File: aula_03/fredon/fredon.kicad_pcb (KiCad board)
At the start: 2 copper layers, 11 parts, among them J1 FRDM-KL25Z, J3 encoder1, J4 encoder2, J5 Conn_01x02_Socket, J6 Conn_01x06_Socket, U1 HC-SR04, U2 NRF24L01_10PIN

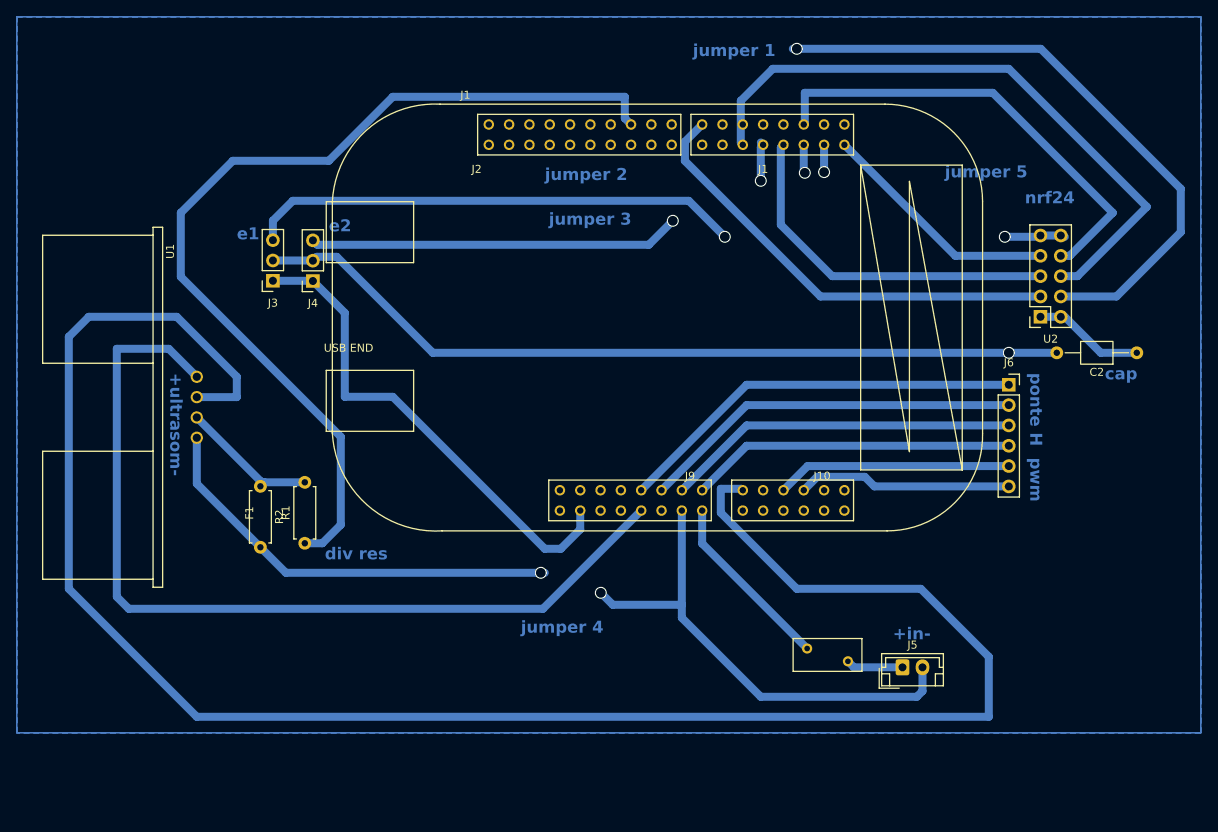
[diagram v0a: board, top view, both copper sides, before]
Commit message: feat(pcb): atualização da pcb para o tamanho de 10x10
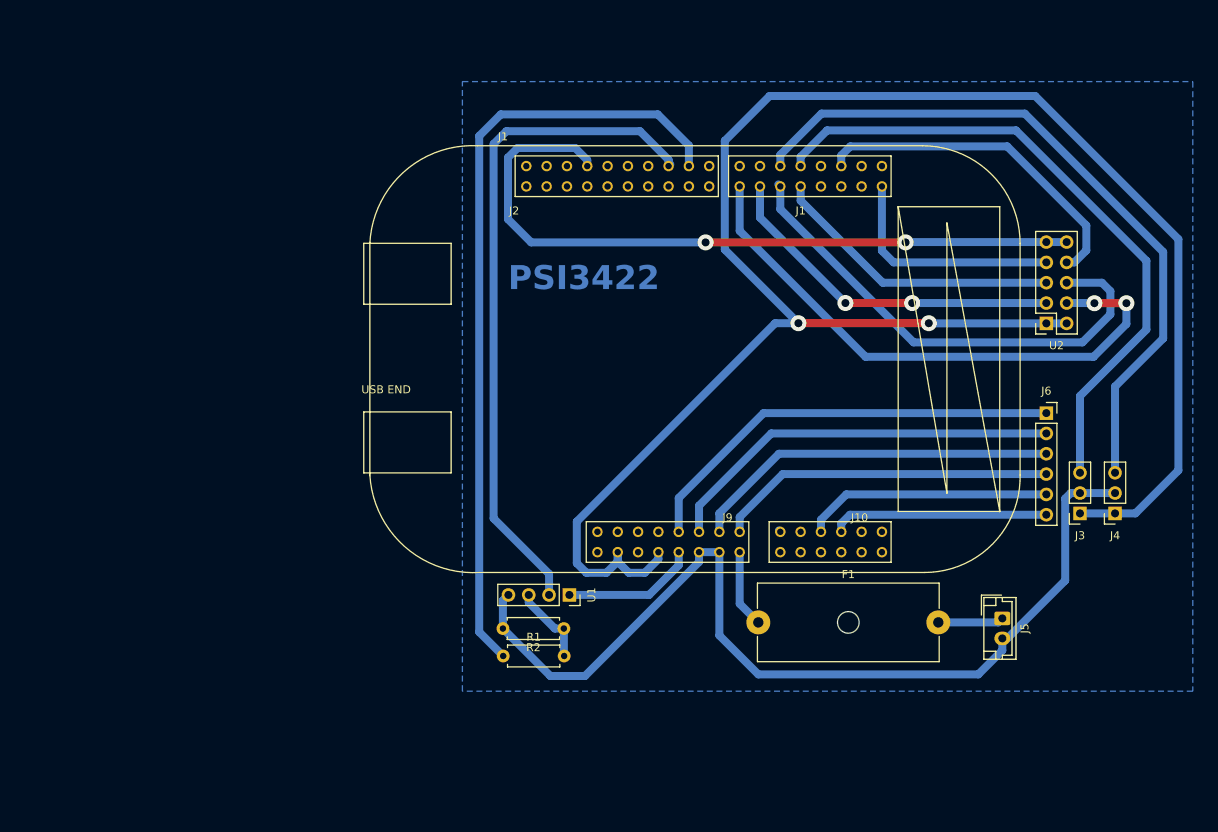
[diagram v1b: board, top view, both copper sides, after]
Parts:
- removed C2: C_Small, Capacitor_THT:C_Axial_L3.8mm_D2.6mm_P10.00mm_Horizontal
- F1: footprint Fuse:Fuse_BelFuse_0ZRE0005FF_L8.3mm_W3.8mm -> Fuse:Fuseholder_Cylinder-5x20mm_Schurter_0031_8201_Horizontal_Open
- U1: footprint HC-SR04:XCVR_HC-SR04 -> Connector_PinSocket_2.54mm:PinSocket_1x04_P2.54mm_Vertical
- moved J3 105.0 mm to (172.9, 102.6)
- moved J4 104.4 mm to (177.3, 102.6)
- moved U1 52.1 mm to (109.1, 112.8)
- moved R2 41.9 mm to (108.4, 117.0), turned to 180 degrees
- moved R1 28.5 mm to (100.8, 120.4), turned to 0 degrees
- moved J5 13.9 mm to (163.2, 115.7), turned to -90 degrees
- moved J1 7.00 mm to (124.5, 83.3)
- moved F1 6.92 mm to (132.7, 116.2)
- moved J6 5.88 mm to (168.7, 90.0)
- moved U2 1.10 mm to (168.7, 78.8)
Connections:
- net Net-(J1-P5V_USB) renamed +5V
- net Net-(J1-PTC6) renamed /PTC6
- net Net-(J1-PTC7) renamed /PTC7
- net Net-(J1-PTD4) renamed /PTD4
- net Net-(J1-PTE2) renamed /PTE2
- net Net-(J1-PTE22) renamed /PTE22
- net Net-(J1-PTE23) renamed /PTE23
- net Net-(J1-PTE3) renamed /PTE3
- net Net-(J1-PTE4) renamed /PTE4
- net Net-(J1-PTE5) renamed /PTE5
- J1 pad J1-10: unconnected-(J1-PTA4-PadJ1-10) -> /PTA4
- J1 pad J1-12: unconnected-(J1-PTA5-PadJ1-12) -> /PTA5
- J1 pad J1-13: unconnected-(J1-PTC10-PadJ1-13) -> /PTC10
- J1 pad J1-15: unconnected-(J1-PTC11-PadJ1-15) -> /PTC11
- J1 pad J1-16: Net-(J1-PTC9) -> unconnected-(J1-PTC9-PadJ1-16)
- J1 pad J1-3: Net-(J1-PTC0) -> unconnected-(J1-PTC0-PadJ1-3)
- J1 pad J1-5: Net-(J1-PTC3) -> unconnected-(J1-PTC3-PadJ1-5)
- J1 pad J1-7: Net-(J1-PTC4) -> unconnected-(J1-PTC4-PadJ1-7)
- J1 pad J1-9: Net-(J1-PTC5) -> /PTC5
- J1 pad J10-1: Net-(J1-PTE20) -> unconnected-(J1-PTE20-PadJ10-1)
- J1 pad J2-4: unconnected-(J1-PTD5-PadJ2-4) -> /PTD5
- J1 pad J2-6: Net-(J1-PTD0) -> /PTD0
- J1 pad J9-4: Net-(J3-Pin_1) -> +3.3V
- J1 pad J9-8: Net-(J3-Pin_1) -> +3.3V
- J3 pad 1: Net-(J3-Pin_1) -> +3.3V
- J3 pad 3: Net-(J1-PTC0) -> /PTA4
- J4 pad 1: Net-(J3-Pin_1) -> +3.3V
- J4 pad 3: Net-(J1-PTC3) -> /PTA5
- R1 pad 1: Net-(J1-PTD0) -> /PTD5
- U1 pad 2: Net-(J1-PTE20) -> /PTD0
- U2 pad 1: Net-(C2-Pad1) -> +3.3V
- U2 pad 2: Net-(C2-Pad1) -> +3.3V
- U2 pad 3: Net-(J1-PTC9) -> /PTC10
- U2 pad 4: Net-(J1-PTC5) -> /PTC11
- U2 pad 5: Net-(J1-PTC4) -> /PTC5
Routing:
- net Net-(J1-PTE20): track 240.1 -> 0.00 mm
- net +3.3V: track 0.00 -> 229.3 mm, vias 0 -> 2
- net Net-(J1-PTD0): track 118.0 -> 0.00 mm
- net /PTD5: track 0.00 -> 97.8 mm
- net +5V: track 113.7 -> 16.8 mm
- net /PTA5: track 0.00 -> 88.7 mm
- net Net-(J1-PTC5): track 84.5 -> 0.00 mm, vias 2 -> 0
- net /PTD0: track 0.00 -> 84.4 mm
- net /PTA4: track 0.00 -> 82.5 mm
- net /PTC11: track 0.00 -> 71.5 mm, vias 0 -> 2
- net Net-(J1-PTC0): track 65.2 -> 0.00 mm, vias 2 -> 0
- net Net-(J3-Pin_1): track 61.8 -> 0.00 mm
- net Net-(J1-PTC9): track 56.9 -> 0.00 mm
- net Net-(J1-PTC3): track 50.0 -> 0.00 mm, vias 2 -> 0
- net Net-(J1-PTC4): track 45.3 -> 0.00 mm
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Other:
- board text added: "PSI3422"
- board text removed: "+in-"
- board text removed: "+ultrasom-"
- board text removed: "cap"
- board text removed: "div res"
- board text removed: "e1"
- board text removed: "e2"
- board text removed: "jumper 1"
- board text removed: "jumper 2"
- board text removed: "jumper 3"
- board text removed: "jumper 4"
- board text removed: "jumper 5"
- board text removed: "nrf24"
- board text removed: "ponte H pwm"

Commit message: revisao da PCB
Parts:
- removed F1: Fuse, Fuse:Fuseholder_Cylinder-5x20mm_Schurter_0031_8201_Horizontal_Open
- U1: footprint Connector_PinSocket_2.54mm:PinSocket_1x04_P2.54mm_Vertical -> HC-SR04:XCVR_HC-SR04
- moved R1 15.8 mm to (116.5, 122.5)
- moved R2 15.8 mm to (124.1, 118.5)
- moved U1 5.60 mm to (111.5, 117.8)
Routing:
- net GND: track 209.8 -> 178.8 mm
- net /PTD5: track 97.8 -> 115.2 mm
- net Net-(U1-ECHO): track 10.1 -> 24.2 mm
- net /PTD0: track 84.4 -> 90.2 mm
- net +5V: track 16.8 -> 14.9 mm
- net +3.3V: track 229.3 -> 228.5 mm
- net Net-(J5-Pin_1): vias 0 -> 1
- net Net-(J1-P5-9V_VIN): vias 0 -> 1
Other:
- board text added: "e1"
- board text added: "e2"
- board text added: "nrf"
- board text added: "ponte H"

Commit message: relatorio
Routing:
- net GND: track 178.8 -> 201.3 mm, vias 2 -> 4
- net Net-(U1-ECHO): track 24.2 -> 18.5 mm
- net /PTD0: track 90.2 -> 91.6 mm
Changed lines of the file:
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@@
 			(at -3.81 0 270)
 			(size 1.53 1.53)
-			(drill 1.02)
+			(drill 0.8)
 			(layers "*.Cu" "*.Mask")
 			(remove_unused_layers no)
@@
 			(at -1.27 0 270)
 			(size 1.53 1.53)
-			(drill 1.02)
+			(drill 0.8)
 			(layers "*.Cu" "*.Mask")
 			(remove_unused_layers no)
@@
 			(at 1.27 0 270)
 			(size 1.53 1.53)
-			(drill 1.02)
+			(drill 0.8)
 			(layers "*.Cu" "*.Mask")
 			(remove_unused_layers no)
@@
 			(at 3.81 0 270)
 			(size 1.53 1.53)
-			(drill 1.02)
+			(drill 0.8)
 			(layers "*.Cu" "*.Mask")
 			(remove_unused_layers no)
@@
 	)
 	(segment
+		(start 125 83)
+		(end 124.5 83)
+		(width 1)
+		(layer "F.Cu")
+		(net 5)
+	)
+	(segment
 		(start 151.1 68.7)
 		(end 126.1 68.7)
 		(width 1)
 		(layer "F.Cu")
+		(net 5)
+	)
+	(segment
+		(start 130 88)
+		(end 125 83)
+		(width 1)
+		(layer "F.Cu")
+		(net 5)
+	)
+	(via
+		(at 130 88)
+		(size 1.5)
+		(drill 0.8)
+		(layers "F.Cu" "B.Cu")
+		(padstack
+			(mode custom)
+			(layer "B.Cu"
+				(size 2)
+			)
+		)
+		(net 5)
+	)
+	(via
+		(at 124.5 83)
+		(size 1.5)
+		(drill 0.8)
+		(layers "F.Cu" "B.Cu")
 		(net 5)
 	)
@@
 	)
 	(segment
+		(start 124.5 70.3)
+		(end 126.1 68.7)
+		(width 1)
+		(layer "B.Cu")
+		(net 5)
+	)
+	(segment
 		(start 101.4 65.8)
 		(end 101.4 58.1)
@@
 	)
 	(segment
+		(start 124.5 83)
+		(end 124.5 70.3)
+		(width 1)
+		(layer "B.Cu")
+		(net 5)
+	)
+	(segment
 		(start 172.925 100.155)
 		(end 172.9 100.13)
@@
 	)
 	(segment
-		(start 111.5 119.08)
-		(end 103.08 119.08)
+		(start 112.42 119.08)
+		(end 115 116.5)
 		(width 1)
 		(layer "B.Cu")
@@
 	)
 	(segment
-		(start 124.12 118.5)
-		(end 128.5 118.5)
+		(start 122.12 116.5)
+		(end 124.12 118.5)
 		(width 1)
 		(layer "B.Cu")
@@
 	)
 	(segment
-		(start 100.763343 113.456793)
-		(end 101.453343 112.766793)
-		(width 1)
-		(layer "B.Cu")
-		(net 35)
-	)
-	(segment
-		(start 103.08 119.08)
-		(end 101 117)
-		(width 1)
-		(layer "B.Cu")
-		(net 35)
-	)
-	(segment
-		(start 100.763343 116.966793)
-		(end 100.763343 113.456793)
+		(start 115 116.5)
+		(end 122.12 116.5)
 		(width 1)
 		(layer "B.Cu")
@@
 		(start 124.12 118.5)
 		(end 124.12 122.5)
+		(width 1)
+		(layer "B.Cu")
+		(net 35)
+	)
+	(segment
+		(start 111.5 119.08)
+		(end 112.42 119.08)
 		(width 1)
 		(layer "B.Cu")
@@
 		(start 110.7 109.5)
 		(end 114.2 109.5)
-		(width 0.7)
+		(width 1)
 		(layer "B.Cu")
 		(net 40)
@@
 		(start 110.5 103.1)
 		(end 110.5 109.3)
-		(width 0.7)
+		(width 1)
 		(layer "B.Cu")
 		(net 40)
@@
 	)
 	(segment
-		(start 106.533343 110.133343)
-		(end 99.6 103.2)
+		(start 121.47 58.37)
+		(end 117.9 54.8)
 		(width 1)
 		(layer "B.Cu")
@@
 	)
 	(segment
+		(start 101.199998 54.8)
+		(end 99.6 56.399998)
+		(width 1)
+		(layer "B.Cu")
+		(net 45)
+	)
+	(segment
+		(start 99.6 107.1)
+		(end 109.04 116.54)
+		(width 1)
+		(layer "B.Cu")
+		(net 45)
+	)
+	(segment
+		(start 109.04 116.54)
+		(end 111.5 116.54)
+		(width 1)
+		(layer "B.Cu")
+		(net 45)
+	)
+	(segment
 		(start 117.9 54.8)
+		(end 101.199998 54.8)
+		(width 1)
+		(layer "B.Cu")
+		(net 45)
+	)
+	(segment
+		(start 121.47 59.16)
 		(end 121.47 58.37)
-		(width 1)
-		(layer "B.Cu")
-		(net 45)
-	)
-	(segment
-		(start 106.533343 110.133343)
-		(end 106.533343 111.033343)
-		(width 1)
-		(layer "B.Cu")
-		(net 45)
-	)
-	(segment
-		(start 109.5 114.54)
-		(end 111.5 116.54)
-		(width 1)
-		(layer "B.Cu")
-		(net 45)
-	)
-	(segment
-		(start 109.5 114)
-		(end 109.5 114.54)
-		(width 1)
-		(layer "B.Cu")
-		(net 45)
-	)
-	(segment
-		(start 121.47 58.37)
-		(end 121.47 59.16)
-		(width 1)
-		(layer "B.Cu")
-		(net 45)
-	)
-	(segment
-		(start 106.533343 111.033343)
-		(end 109.5 114)
-		(width 1)
-		(layer "B.Cu")
-		(net 45)
-	)
-	(segment
-		(start 99.6 103.2)
-		(end 99.6 56.399998)
-		(width 1)
-		(layer "B.Cu")
-		(net 45)
-	)
-	(segment
-		(start 99.6 56.399998)
-		(end 101.199998 54.8)
 		(width 1)
 		(layer "B.Cu")
@@
 	)
 	(segment
-		(start 101.199998 54.8)
-		(end 117.9 54.8)
+		(start 99.6 56.399998)
+		(end 99.6 107.1)
 		(width 1)
 		(layer "B.Cu")
@@
 		(polygon
 			(pts
-				(xy 95.5 49) (xy 187 48.5) (xy 187 125) (xy 95.5 125)
-			)
-		)
+				(xy 96 49) (xy 187.5 48.5) (xy 187 125.5) (xy 95 125.5) (xy 96.5 49)
+			)
+		)
